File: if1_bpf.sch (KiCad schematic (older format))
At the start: 8 parts

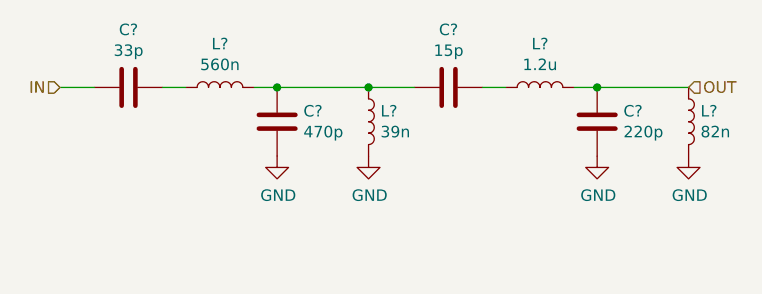
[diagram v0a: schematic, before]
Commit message: IF1 BPF updated
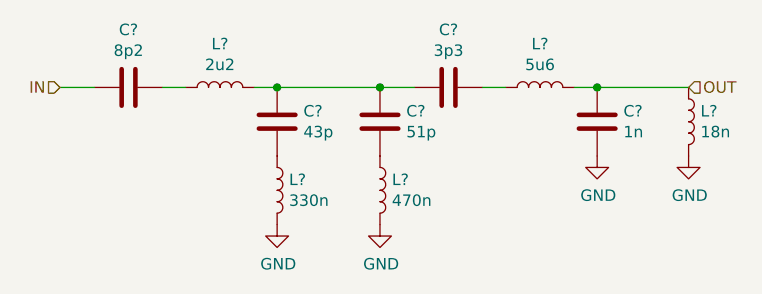
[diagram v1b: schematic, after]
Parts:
- added C?: 51p, symbol Device:C
- added L?: 470n, symbol Device:L
- C?: value 33p -> 8p2
- C?: value 470p -> 43p
- C?: value 15p -> 3p3
- C?: value 220p -> 1n
- L?: value 560n -> 2u2
- L?: value 39n -> 330n
- L?: value 1.2u -> 5u6
- L?: value 82n -> 18n
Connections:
- net GND: now also L?.2; no longer C?.1
- net at C?.2, C?.2, L?.1: now also C?.2; no longer L?.1
- new net: C?.1, L?.1 (x2)
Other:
- moved on the sheet: L?
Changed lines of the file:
@@
 P 3250 2000
 F 0 "C?" V 2998 2000 50  0000 C CNN
-F 1 "33p" V 3089 2000 50  0000 C CNN
+F 1 "8p2" V 3089 2000 50  0000 C CNN
 F 2 "" H 3288 1850 50  0001 C CNN
 F 3 "~" H 3250 2000 50  0001 C CNN
@@
 P 3650 2000
 F 0 "L?" V 3840 2000 50  0000 C CNN
-F 1 "560n" V 3749 2000 50  0000 C CNN
+F 1 "2u2" V 3749 2000 50  0000 C CNN
 F 2 "" H 3650 2000 50  0001 C CNN
 F 3 "~" H 3650 2000 50  0001 C CNN
@@
 P 3900 2150
 F 0 "C?" H 3785 2104 50  0000 R CNN
-F 1 "470p" H 3785 2195 50  0000 R CNN
+F 1 "43p" H 3785 2195 50  0000 R CNN
 F 2 "" H 3938 2000 50  0001 C CNN
 F 3 "~" H 3900 2150 50  0001 C CNN
@@
 L Device:L L?
 U 1 1 5FE75044
-P 4300 2150
-F 0 "L?" H 4352 2196 50  0000 L CNN
-F 1 "39n" H 4352 2105 50  0000 L CNN
-F 2 "" H 4300 2150 50  0001 C CNN
-F 3 "~" H 4300 2150 50  0001 C CNN
-	1    4300 2150
+P 3900 2450
+F 0 "L?" H 3952 2496 50  0000 L CNN
+F 1 "330n" H 3952 2405 50  0000 L CNN
+F 2 "" H 3900 2450 50  0001 C CNN
+F 3 "~" H 3900 2450 50  0001 C CNN
+	1    3900 2450
 	1    0    0    -1
 $EndComp
@@
 P 4650 2000
 F 0 "C?" V 4398 2000 50  0000 C CNN
-F 1 "15p" V 4489 2000 50  0000 C CNN
+F 1 "3p3" V 4489 2000 50  0000 C CNN
 F 2 "" H 4688 1850 50  0001 C CNN
 F 3 "~" H 4650 2000 50  0001 C CNN
@@
 P 5050 2000
 F 0 "L?" V 5240 2000 50  0000 C CNN
-F 1 "1.2u" V 5149 2000 50  0000 C CNN
+F 1 "5u6" V 5149 2000 50  0000 C CNN
 F 2 "" H 5050 2000 50  0001 C CNN
 F 3 "~" H 5050 2000 50  0001 C CNN
@@
 P 5700 2150
 F 0 "L?" H 5752 2196 50  0000 L CNN
-F 1 "82n" H 5752 2105 50  0000 L CNN
+F 1 "18n" H 5752 2105 50  0000 L CNN
 F 2 "" H 5700 2150 50  0001 C CNN
 F 3 "~" H 5700 2150 50  0001 C CNN
@@
 P 5300 2150
 F 0 "C?" H 5185 2104 50  0000 R CNN
-F 1 "220p" H 5185 2195 50  0000 R CNN
+F 1 "1n" H 5185 2195 50  0000 R CNN
 F 2 "" H 5338 2000 50  0001 C CNN
 F 3 "~" H 5300 2150 50  0001 C CNN
@@
 Connection ~ 3900 2000
 Wire Wire Line
-	3900 2000 4300 2000
-Connection ~ 4300 2000
-Wire Wire Line
-	4300 2000 4500 2000
-Wire Wire Line
 	4800 2000 4900 2000
 Wire Wire Line
@@
 $Comp
 L power:GND #PWR?
-U 1 1 5FE7C471
-P 3900 2300
-F 0 "#PWR?" H 3900 2050 50  0001 C CNN
-F 1 "GND" H 3905 2127 50  0000 C CNN
-F 2 "" H 3900 2300 50  0001 C CNN
-F 3 "" H 3900 2300 50  0001 C CNN
-	1    3900 2300
-	1    0    0    -1
-$EndComp
-$Comp
-L power:GND #PWR?
 U 1 1 5FE7C8C8
-P 4300 2300
-F 0 "#PWR?" H 4300 2050 50  0001 C CNN
-F 1 "GND" H 4305 2127 50  0000 C CNN
-F 2 "" H 4300 2300 50  0001 C CNN
-F 3 "" H 4300 2300 50  0001 C CNN
-	1    4300 2300
+P 3900 2600
+F 0 "#PWR?" H 3900 2350 50  0001 C CNN
+F 1 "GND" H 3905 2427 50  0000 C CNN
+F 2 "" H 3900 2600 50  0001 C CNN
+F 3 "" H 3900 2600 50  0001 C CNN
+	1    3900 2600
 	1    0    0    -1
 $EndComp
@@
 Text HLabel 5700 2000 2    50   Input ~ 0
 OUT
+Wire Wire Line
+	3900 2000 4350 2000
+$Comp
+L Device:C C?
+U 1 1 5FE92C59
+P 4350 2150
+F 0 "C?" H 4235 2104 50  0000 R CNN
+F 1 "51p" H 4235 2195 50  0000 R CNN
+F 2 "" H 4388 2000 50  0001 C CNN
+F 3 "~" H 4350 2150 50  0001 C CNN
+	1    4350 2150
+	-1   0    0    1
+$EndComp
+$Comp
+L Device:L L?
+U 1 1 5FE92D35
+P 4350 2450
+F 0 "L?" H 4402 2496 50  0000 L CNN
+F 1 "470n" H 4402 2405 50  0000 L CNN
+F 2 "" H 4350 2450 50  0001 C CNN
+F 3 "~" H 4350 2450 50  0001 C CNN
+	1    4350 2450
+	1    0    0    -1
+$EndComp
+$Comp
+L power:GND #PWR?
+U 1 1 5FE92D3F
+P 4350 2600
+F 0 "#PWR?" H 4350 2350 50  0001 C CNN
+F 1 "GND" H 4355 2427 50  0000 C CNN
+F 2 "" H 4350 2600 50  0001 C CNN
+F 3 "" H 4350 2600 50  0001 C CNN
+	1    4350 2600
+	1    0    0    -1
+$EndComp
+Connection ~ 4350 2000
+Wire Wire Line
+	4350 2000 4500 2000
 $EndSCHEMATC

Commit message: Initalize receiver test circuit
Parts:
- gave numbers to parts that had none: 10
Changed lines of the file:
@@
 $Descr A4 11693 8268
 encoding utf-8
-Sheet 3 9
+Sheet 3 7
 Title ""
 Date ""
@@
 $EndDescr
 $Comp
-L Device:C C?
+L Device:C C5
 U 1 1 5FE7343E
 P 3250 2000
-F 0 "C?" V 2998 2000 50  0000 C CNN
+F 0 "C5" V 2998 2000 50  0000 C CNN
 F 1 "8p2" V 3089 2000 50  0000 C CNN
 F 2 "" H 3288 1850 50  0001 C CNN
@@
 $EndComp
 $Comp
-L Device:L L?
+L Device:L L4
 U 1 1 5FE73D0E
 P 3650 2000
-F 0 "L?" V 3840 2000 50  0000 C CNN
+F 0 "L4" V 3840 2000 50  0000 C CNN
 F 1 "2u2" V 3749 2000 50  0000 C CNN
 F 2 "" H 3650 2000 50  0001 C CNN
@@
 $EndComp
 $Comp
-L Device:C C?
+L Device:C C6
 U 1 1 5FE74A56
 P 3900 2150
-F 0 "C?" H 3785 2104 50  0000 R CNN
+F 0 "C6" H 3785 2104 50  0000 R CNN
 F 1 "43p" H 3785 2195 50  0000 R CNN
 F 2 "" H 3938 2000 50  0001 C CNN
@@
 $EndComp
 $Comp
-L Device:L L?
+L Device:L L5
 U 1 1 5FE75044
 P 3900 2450
-F 0 "L?" H 3952 2496 50  0000 L CNN
+F 0 "L5" H 3952 2496 50  0000 L CNN
 F 1 "330n" H 3952 2405 50  0000 L CNN
 F 2 "" H 3900 2450 50  0001 C CNN
@@
 $EndComp
 $Comp
-L Device:C C?
+L Device:C C8
 U 1 1 5FE756D3
 P 4650 2000
-F 0 "C?" V 4398 2000 50  0000 C CNN
+F 0 "C8" V 4398 2000 50  0000 C CNN
 F 1 "3p3" V 4489 2000 50  0000 C CNN
 F 2 "" H 4688 1850 50  0001 C CNN
@@
 $EndComp
 $Comp
-L Device:L L?
+L Device:L L7
 U 1 1 5FE771FA
 P 5050 2000
-F 0 "L?" V 5240 2000 50  0000 C CNN
+F 0 "L7" V 5240 2000 50  0000 C CNN
 F 1 "5u6" V 5149 2000 50  0000 C CNN
 F 2 "" H 5050 2000 50  0001 C CNN
@@
 $EndComp
 $Comp
-L Device:L L?
+L Device:L L8
 U 1 1 5FE79301
 P 5700 2150
-F 0 "L?" H 5752 2196 50  0000 L CNN
+F 0 "L8" H 5752 2196 50  0000 L CNN
 F 1 "18n" H 5752 2105 50  0000 L CNN
 F 2 "" H 5700 2150 50  0001 C CNN
@@
 $EndComp
 $Comp
-L Device:C C?
+L Device:C C9
 U 1 1 5FE792FB
 P 5300 2150
-F 0 "C?" H 5185 2104 50  0000 R CNN
+F 0 "C9" H 5185 2104 50  0000 R CNN
 F 1 "1n" H 5185 2195 50  0000 R CNN
 F 2 "" H 5338 2000 50  0001 C CNN
@@
 	5300 2000 5700 2000
 $Comp
-L power:GND #PWR?
+L power:GND #PWR0108
 U 1 1 5FE7C8C8
 P 3900 2600
-F 0 "#PWR?" H 3900 2350 50  0001 C CNN
+F 0 "#PWR0108" H 3900 2350 50  0001 C CNN
 F 1 "GND" H 3905 2427 50  0000 C CNN
 F 2 "" H 3900 2600 50  0001 C CNN
@@
 $EndComp
 $Comp
-L power:GND #PWR?
+L power:GND #PWR0109
 U 1 1 5FE7CE31
 P 5300 2300
-F 0 "#PWR?" H 5300 2050 50  0001 C CNN
+F 0 "#PWR0109" H 5300 2050 50  0001 C CNN
 F 1 "GND" H 5305 2127 50  0000 C CNN
 F 2 "" H 5300 2300 50  0001 C CNN
@@
 $EndComp
 $Comp
-L power:GND #PWR?
+L power:GND #PWR0110
 U 1 1 5FE7D2D1
 P 5700 2300
-F 0 "#PWR?" H 5700 2050 50  0001 C CNN
+F 0 "#PWR0110" H 5700 2050 50  0001 C CNN
 F 1 "GND" H 5705 2127 50  0000 C CNN
 F 2 "" H 5700 2300 50  0001 C CNN
@@
 	3900 2000 4350 2000
 $Comp
-L Device:C C?
+L Device:C C7
 U 1 1 5FE92C59
 P 4350 2150
-F 0 "C?" H 4235 2104 50  0000 R CNN
+F 0 "C7" H 4235 2104 50  0000 R CNN
 F 1 "51p" H 4235 2195 50  0000 R CNN
 F 2 "" H 4388 2000 50  0001 C CNN
@@
 $EndComp
 $Comp
-L Device:L L?
+L Device:L L6
 U 1 1 5FE92D35
 P 4350 2450
-F 0 "L?" H 4402 2496 50  0000 L CNN
+F 0 "L6" H 4402 2496 50  0000 L CNN
 F 1 "470n" H 4402 2405 50  0000 L CNN
 F 2 "" H 4350 2450 50  0001 C CNN
@@
 $EndComp
 $Comp
-L power:GND #PWR?
+L power:GND #PWR0111
 U 1 1 5FE92D3F
 P 4350 2600
-F 0 "#PWR?" H 4350 2350 50  0001 C CNN
+F 0 "#PWR0111" H 4350 2350 50  0001 C CNN
 F 1 "GND" H 4355 2427 50  0000 C CNN
 F 2 "" H 4350 2600 50  0001 C CNN

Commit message: Nyáktervezésre majdnem kész
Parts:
- C5, C6, C7, C8, C9: footprint (none) -> Capacitor_SMD:C_0805_2012Metric_Pad1.15x1.40mm_HandSolder
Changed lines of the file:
@@
 F 0 "C5" V 2998 2000 50  0000 C CNN
 F 1 "8p2" V 3089 2000 50  0000 C CNN
-F 2 "" H 3288 1850 50  0001 C CNN
+F 2 "Capacitor_SMD:C_0805_2012Metric_Pad1.15x1.40mm_HandSolder" H 3288 1850 50  0001 C CNN
 F 3 "~" H 3250 2000 50  0001 C CNN
 	1    3250 2000
@@
 F 0 "C6" H 3785 2104 50  0000 R CNN
 F 1 "43p" H 3785 2195 50  0000 R CNN
-F 2 "" H 3938 2000 50  0001 C CNN
+F 2 "Capacitor_SMD:C_0805_2012Metric_Pad1.15x1.40mm_HandSolder" H 3938 2000 50  0001 C CNN
 F 3 "~" H 3900 2150 50  0001 C CNN
 	1    3900 2150
@@
 F 0 "C8" V 4398 2000 50  0000 C CNN
 F 1 "3p3" V 4489 2000 50  0000 C CNN
-F 2 "" H 4688 1850 50  0001 C CNN
+F 2 "Capacitor_SMD:C_0805_2012Metric_Pad1.15x1.40mm_HandSolder" H 4688 1850 50  0001 C CNN
 F 3 "~" H 4650 2000 50  0001 C CNN
 	1    4650 2000
@@
 F 0 "C9" H 5185 2104 50  0000 R CNN
 F 1 "1n" H 5185 2195 50  0000 R CNN
-F 2 "" H 5338 2000 50  0001 C CNN
+F 2 "Capacitor_SMD:C_0805_2012Metric_Pad1.15x1.40mm_HandSolder" H 5338 2000 50  0001 C CNN
 F 3 "~" H 5300 2150 50  0001 C CNN
 	1    5300 2150
@@
 F 0 "C7" H 4235 2104 50  0000 R CNN
 F 1 "51p" H 4235 2195 50  0000 R CNN
-F 2 "" H 4388 2000 50  0001 C CNN
+F 2 "Capacitor_SMD:C_0805_2012Metric_Pad1.15x1.40mm_HandSolder" H 4388 2000 50  0001 C CNN
 F 3 "~" H 4350 2150 50  0001 C CNN
 	1    4350 2150

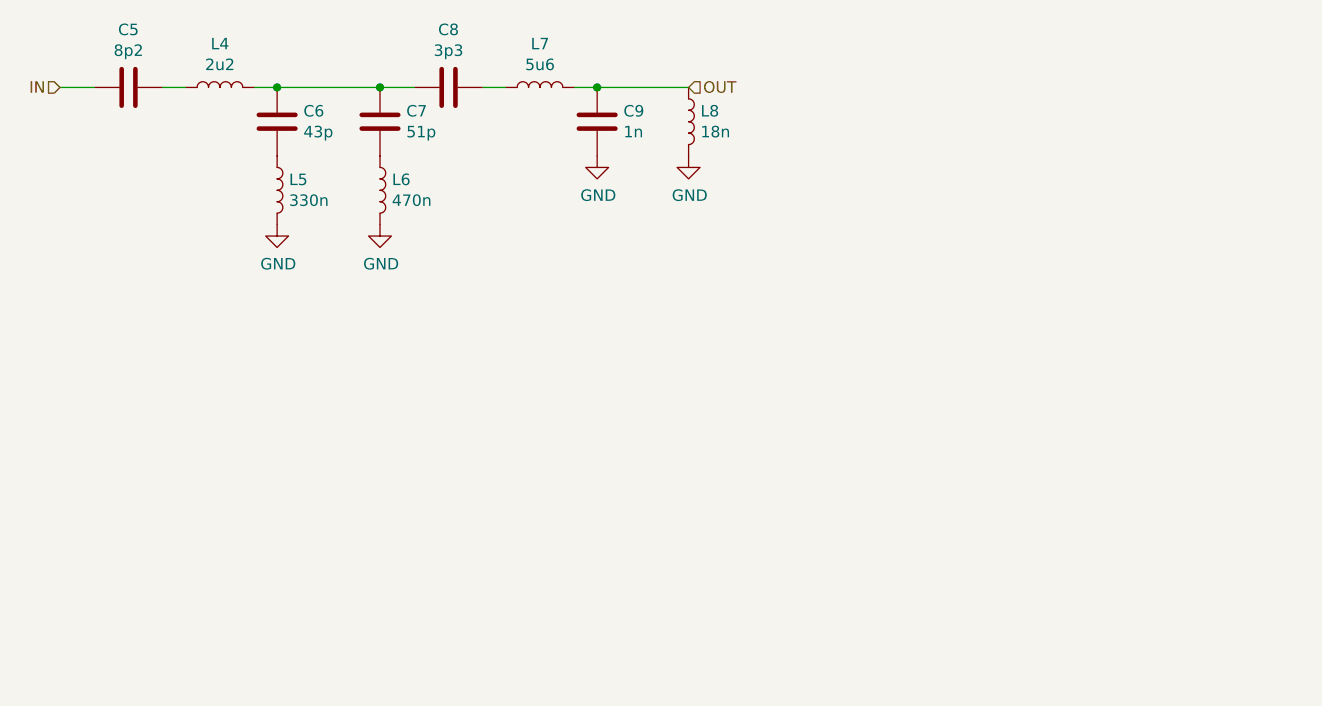
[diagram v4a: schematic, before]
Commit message: Receiver test panel ++
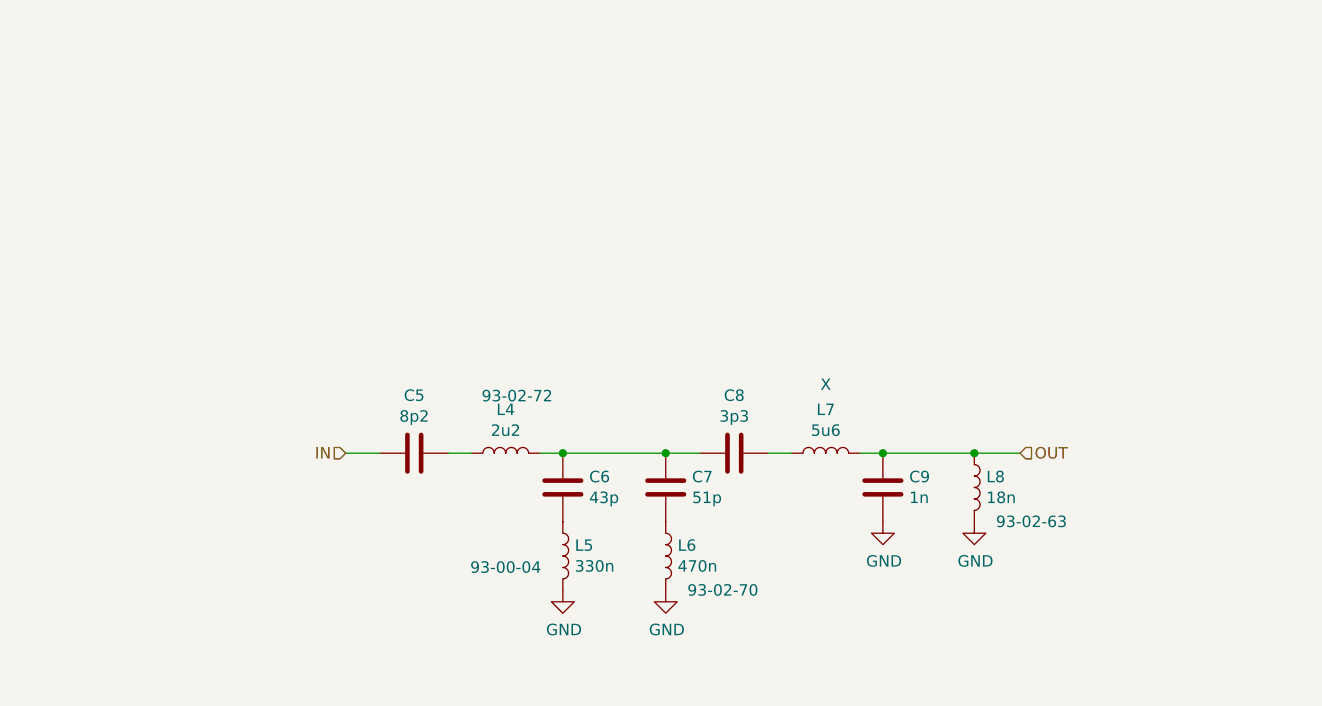
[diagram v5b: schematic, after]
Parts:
- L4: footprint (none) -> Inductor_SMD:L_0805_2012Metric_Pad1.15x1.40mm_HandSolder; Lomex (none) -> 93-02-72
- L5: footprint (none) -> Inductor_SMD:L_1210_3225Metric_Pad1.42x2.65mm_HandSolder; Lomex (none) -> 93-00-04
- L6: footprint (none) -> Inductor_SMD:L_0805_2012Metric_Pad1.15x1.40mm_HandSolder; Lomex (none) -> 93-02-70
- L7: Lomex (none) -> X
- L8: footprint (none) -> Inductor_SMD:L_0402_1005Metric_Pad0.77x0.64mm_HandSolder; Lomex (none) -> 93-02-63
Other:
- moved on the sheet: C5, C6, C7, C8, C9, L4, L5, L6, L7, L8
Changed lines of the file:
@@
 encoding utf-8
 Sheet 3 7
-Title ""
-Date ""
+Title "37 MHz IF Filter"
+Date "2021-01-15"
 Rev ""
-Comp ""
+Comp "HA5KFU"
 Comment1 ""
 Comment2 ""
@@
 L Device:C C5
 U 1 1 5FE7343E
-P 3250 2000
-F 0 "C5" V 2998 2000 50  0000 C CNN
-F 1 "8p2" V 3089 2000 50  0000 C CNN
-F 2 "Capacitor_SMD:C_0805_2012Metric_Pad1.15x1.40mm_HandSolder" H 3288 1850 50  0001 C CNN
-F 3 "~" H 3250 2000 50  0001 C CNN
-	1    3250 2000
+P 4500 3600
+F 0 "C5" V 4248 3600 50  0000 C CNN
+F 1 "8p2" V 4339 3600 50  0000 C CNN
+F 2 "Capacitor_SMD:C_0805_2012Metric_Pad1.15x1.40mm_HandSolder" H 4538 3450 50  0001 C CNN
+F 3 "~" H 4500 3600 50  0001 C CNN
+	1    4500 3600
 	0    1    1    0
 $EndComp
@@
 L Device:L L4
 U 1 1 5FE73D0E
-P 3650 2000
-F 0 "L4" V 3840 2000 50  0000 C CNN
-F 1 "2u2" V 3749 2000 50  0000 C CNN
-F 2 "" H 3650 2000 50  0001 C CNN
-F 3 "~" H 3650 2000 50  0001 C CNN
-	1    3650 2000
+P 4900 3600
+F 0 "L4" V 5090 3600 50  0000 C CNN
+F 1 "2u2" V 4999 3600 50  0000 C CNN
+F 2 "Inductor_SMD:L_0805_2012Metric_Pad1.15x1.40mm_HandSolder" H 4900 3600 50  0001 C CNN
+F 3 "~" H 4900 3600 50  0001 C CNN
+F 4 "93-02-72 " V 5150 3650 50  0000 C CNN "Lomex"
+	1    4900 3600
 	0    1    -1   0
 $EndComp
@@
 L Device:C C6
 U 1 1 5FE74A56
-P 3900 2150
-F 0 "C6" H 3785 2104 50  0000 R CNN
-F 1 "43p" H 3785 2195 50  0000 R CNN
-F 2 "Capacitor_SMD:C_0805_2012Metric_Pad1.15x1.40mm_HandSolder" H 3938 2000 50  0001 C CNN
-F 3 "~" H 3900 2150 50  0001 C CNN
-	1    3900 2150
+P 5150 3750
+F 0 "C6" H 5035 3704 50  0000 R CNN
+F 1 "43p" H 5035 3795 50  0000 R CNN
+F 2 "Capacitor_SMD:C_0805_2012Metric_Pad1.15x1.40mm_HandSolder" H 5188 3600 50  0001 C CNN
+F 3 "~" H 5150 3750 50  0001 C CNN
+	1    5150 3750
 	-1   0    0    1
 $EndComp
@@
 L Device:L L5
 U 1 1 5FE75044
-P 3900 2450
-F 0 "L5" H 3952 2496 50  0000 L CNN
-F 1 "330n" H 3952 2405 50  0000 L CNN
-F 2 "" H 3900 2450 50  0001 C CNN
-F 3 "~" H 3900 2450 50  0001 C CNN
-	1    3900 2450
+P 5150 4050
+F 0 "L5" H 5202 4096 50  0000 L CNN
+F 1 "330n" H 5202 4005 50  0000 L CNN
+F 2 "Inductor_SMD:L_1210_3225Metric_Pad1.42x2.65mm_HandSolder" H 5150 4050 50  0001 C CNN
+F 3 "~" H 5150 4050 50  0001 C CNN
+F 4 "93-00-04" H 4900 4000 50  0000 C CNN "Lomex"
+	1    5150 4050
 	1    0    0    -1
 $EndComp
@@
 L Device:C C8
 U 1 1 5FE756D3
-P 4650 2000
-F 0 "C8" V 4398 2000 50  0000 C CNN
-F 1 "3p3" V 4489 2000 50  0000 C CNN
-F 2 "Capacitor_SMD:C_0805_2012Metric_Pad1.15x1.40mm_HandSolder" H 4688 1850 50  0001 C CNN
-F 3 "~" H 4650 2000 50  0001 C CNN
-	1    4650 2000
+P 5900 3600
+F 0 "C8" V 5648 3600 50  0000 C CNN
+F 1 "3p3" V 5739 3600 50  0000 C CNN
+F 2 "Capacitor_SMD:C_0805_2012Metric_Pad1.15x1.40mm_HandSolder" H 5938 3450 50  0001 C CNN
+F 3 "~" H 5900 3600 50  0001 C CNN
+	1    5900 3600
 	0    1    1    0
 $EndComp
@@
 L Device:L L7
 U 1 1 5FE771FA
-P 5050 2000
-F 0 "L7" V 5240 2000 50  0000 C CNN
-F 1 "5u6" V 5149 2000 50  0000 C CNN
-F 2 "" H 5050 2000 50  0001 C CNN
-F 3 "~" H 5050 2000 50  0001 C CNN
-	1    5050 2000
+P 6300 3600
+F 0 "L7" V 6490 3600 50  0000 C CNN
+F 1 "5u6" V 6399 3600 50  0000 C CNN
+F 2 "" H 6300 3600 50  0001 C CNN
+F 3 "~" H 6300 3600 50  0001 C CNN
+F 4 "X" V 6600 3600 50  0000 C CNN "Lomex"
+	1    6300 3600
 	0    1    -1   0
 $EndComp
@@
 L Device:L L8
 U 1 1 5FE79301
-P 5700 2150
-F 0 "L8" H 5752 2196 50  0000 L CNN
-F 1 "18n" H 5752 2105 50  0000 L CNN
-F 2 "" H 5700 2150 50  0001 C CNN
-F 3 "~" H 5700 2150 50  0001 C CNN
-	1    5700 2150
+P 6950 3750
+F 0 "L8" H 7002 3796 50  0000 L CNN
+F 1 "18n" H 7002 3705 50  0000 L CNN
+F 2 "Inductor_SMD:L_0402_1005Metric_Pad0.77x0.64mm_HandSolder" H 6950 3750 50  0001 C CNN
+F 3 "~" H 6950 3750 50  0001 C CNN
+F 4 "93-02-63" H 7200 3600 50  0000 C CNN "Lomex"
+	1    6950 3750
 	1    0    0    -1
 $EndComp
@@
 L Device:C C9
 U 1 1 5FE792FB
-P 5300 2150
-F 0 "C9" H 5185 2104 50  0000 R CNN
-F 1 "1n" H 5185 2195 50  0000 R CNN
-F 2 "Capacitor_SMD:C_0805_2012Metric_Pad1.15x1.40mm_HandSolder" H 5338 2000 50  0001 C CNN
-F 3 "~" H 5300 2150 50  0001 C CNN
-	1    5300 2150
+P 6550 3750
+F 0 "C9" H 6435 3704 50  0000 R CNN
+F 1 "1n" H 6435 3795 50  0000 R CNN
+F 2 "Capacitor_SMD:C_0805_2012Metric_Pad1.15x1.40mm_HandSolder" H 6588 3600 50  0001 C CNN
+F 3 "~" H 6550 3750 50  0001 C CNN
+	1    6550 3750
 	-1   0    0    1
 $EndComp
 Wire Wire Line
-	2950 2000 3100 2000
+	4200 3600 4350 3600
 Wire Wire Line
-	3400 2000 3500 2000
+	4650 3600 4750 3600
 Wire Wire Line
-	3800 2000 3900 2000
-Connection ~ 3900 2000
+	5050 3600 5150 3600
+Connection ~ 5150 3600
 Wire Wire Line
-	4800 2000 4900 2000
+	6050 3600 6150 3600
 Wire Wire Line
-	5200 2000 5300 2000
-Connection ~ 5300 2000
+	6450 3600 6550 3600
+Connection ~ 6550 3600
 Wire Wire Line
-	5300 2000 5700 2000
+	6550 3600 6950 3600
 $Comp
 L power:GND #PWR0108
 U 1 1 5FE7C8C8
-P 3900 2600
-F 0 "#PWR0108" H 3900 2350 50  0001 C CNN
-F 1 "GND" H 3905 2427 50  0000 C CNN
-F 2 "" H 3900 2600 50  0001 C CNN
-F 3 "" H 3900 2600 50  0001 C CNN
-	1    3900 2600
+P 5150 4200
+F 0 "#PWR0108" H 5150 3950 50  0001 C CNN
+F 1 "GND" H 5155 4027 50  0000 C CNN
+F 2 "" H 5150 4200 50  0001 C CNN
+F 3 "" H 5150 4200 50  0001 C CNN
+	1    5150 4200
 	1    0    0    -1
 $EndComp
@@
 L power:GND #PWR0109
 U 1 1 5FE7CE31
-P 5300 2300
-F 0 "#PWR0109" H 5300 2050 50  0001 C CNN
-F 1 "GND" H 5305 2127 50  0000 C CNN
-F 2 "" H 5300 2300 50  0001 C CNN
-F 3 "" H 5300 2300 50  0001 C CNN
-	1    5300 2300
+P 6550 3900
+F 0 "#PWR0109" H 6550 3650 50  0001 C CNN
+F 1 "GND" H 6555 3727 50  0000 C CNN
+F 2 "" H 6550 3900 50  0001 C CNN
+F 3 "" H 6550 3900 50  0001 C CNN
+	1    6550 3900
 	1    0    0    -1
 $EndComp
@@
 L power:GND #PWR0110
 U 1 1 5FE7D2D1
-P 5700 2300
-F 0 "#PWR0110" H 5700 2050 50  0001 C CNN
-F 1 "GND" H 5705 2127 50  0000 C CNN
-F 2 "" H 5700 2300 50  0001 C CNN
-F 3 "" H 5700 2300 50  0001 C CNN
-	1    5700 2300
+P 6950 3900
+F 0 "#PWR0110" H 6950 3650 50  0001 C CNN
+F 1 "GND" H 6955 3727 50  0000 C CNN
+F 2 "" H 6950 3900 50  0001 C CNN
+F 3 "" H 6950 3900 50  0001 C CNN
+	1    6950 3900
 	1    0    0    -1
 $EndComp
-Text HLabel 2950 2000 0    50   Input ~ 0
+Text HLabel 4200 3600 0    50   Input ~ 0
 IN
-Text HLabel 5700 2000 2    50   Input ~ 0
+Text HLabel 7150 3600 2    50   Input ~ 0
 OUT
 Wire Wire Line
-	3900 2000 4350 2000
+	5150 3600 5600 3600
 $Comp
 L Device:C C7
 U 1 1 5FE92C59
-P 4350 2150
-F 0 "C7" H 4235 2104 50  0000 R CNN
-F 1 "51p" H 4235 2195 50  0000 R CNN
-F 2 "Capacitor_SMD:C_0805_2012Metric_Pad1.15x1.40mm_HandSolder" H 4388 2000 50  0001 C CNN
-F 3 "~" H 4350 2150 50  0001 C CNN
-	1    4350 2150
+P 5600 3750
+F 0 "C7" H 5485 3704 50  0000 R CNN
+F 1 "51p" H 5485 3795 50  0000 R CNN
+F 2 "Capacitor_SMD:C_0805_2012Metric_Pad1.15x1.40mm_HandSolder" H 5638 3600 50  0001 C CNN
+F 3 "~" H 5600 3750 50  0001 C CNN
+	1    5600 3750
 	-1   0    0    1
 $EndComp
@@
 L Device:L L6
 U 1 1 5FE92D35
-P 4350 2450
-F 0 "L6" H 4402 2496 50  0000 L CNN
-F 1 "470n" H 4402 2405 50  0000 L CNN
-F 2 "" H 4350 2450 50  0001 C CNN
-F 3 "~" H 4350 2450 50  0001 C CNN
-	1    4350 2450
+P 5600 4050
+F 0 "L6" H 5652 4096 50  0000 L CNN
+F 1 "470n" H 5652 4005 50  0000 L CNN
+F 2 "Inductor_SMD:L_0805_2012Metric_Pad1.15x1.40mm_HandSolder" H 5600 4050 50  0001 C CNN
+F 3 "~" H 5600 4050 50  0001 C CNN
+F 4 "93-02-70" H 5850 3900 50  0000 C CNN "Lomex"
+	1    5600 4050
 	1    0    0    -1
 $EndComp
@@
 L power:GND #PWR0111
 U 1 1 5FE92D3F
-P 4350 2600
-F 0 "#PWR0111" H 4350 2350 50  0001 C CNN
-F 1 "GND" H 4355 2427 50  0000 C CNN
-F 2 "" H 4350 2600 50  0001 C CNN
-F 3 "" H 4350 2600 50  0001 C CNN
-	1    4350 2600
+P 5600 4200
+F 0 "#PWR0111" H 5600 3950 50  0001 C CNN
+F 1 "GND" H 5605 4027 50  0000 C CNN
+F 2 "" H 5600 4200 50  0001 C CNN
+F 3 "" H 5600 4200 50  0001 C CNN
+	1    5600 4200
 	1    0    0    -1
 $EndComp
-Connection ~ 4350 2000
+Connection ~ 5600 3600
 Wire Wire Line
-	4350 2000 4500 2000
+	5600 3600 5750 3600
+Wire Wire Line
+	7150 3600 6950 3600
+Connection ~ 6950 3600
 $EndSCHEMATC
